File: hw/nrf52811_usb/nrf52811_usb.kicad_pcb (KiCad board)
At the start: 2 copper layers, 80 x 65 mm, 93 parts, among them J1 windrain, J10 Solar Panel, J2 RP_SMA, J3 UART, J4 Battery, J5 Power, J7 AM2315, J8 TC2030-CTX, J9 Therm, Q1 Q_PMOS_GSD, SW1 RST, SW2 RST, U1 MIC550X, U2 NRF52811-QFAA, U3 XBEE_S2C, U5 BMP280, U6 MCP73871, Y1 32.768kHz, Y2 32MHz

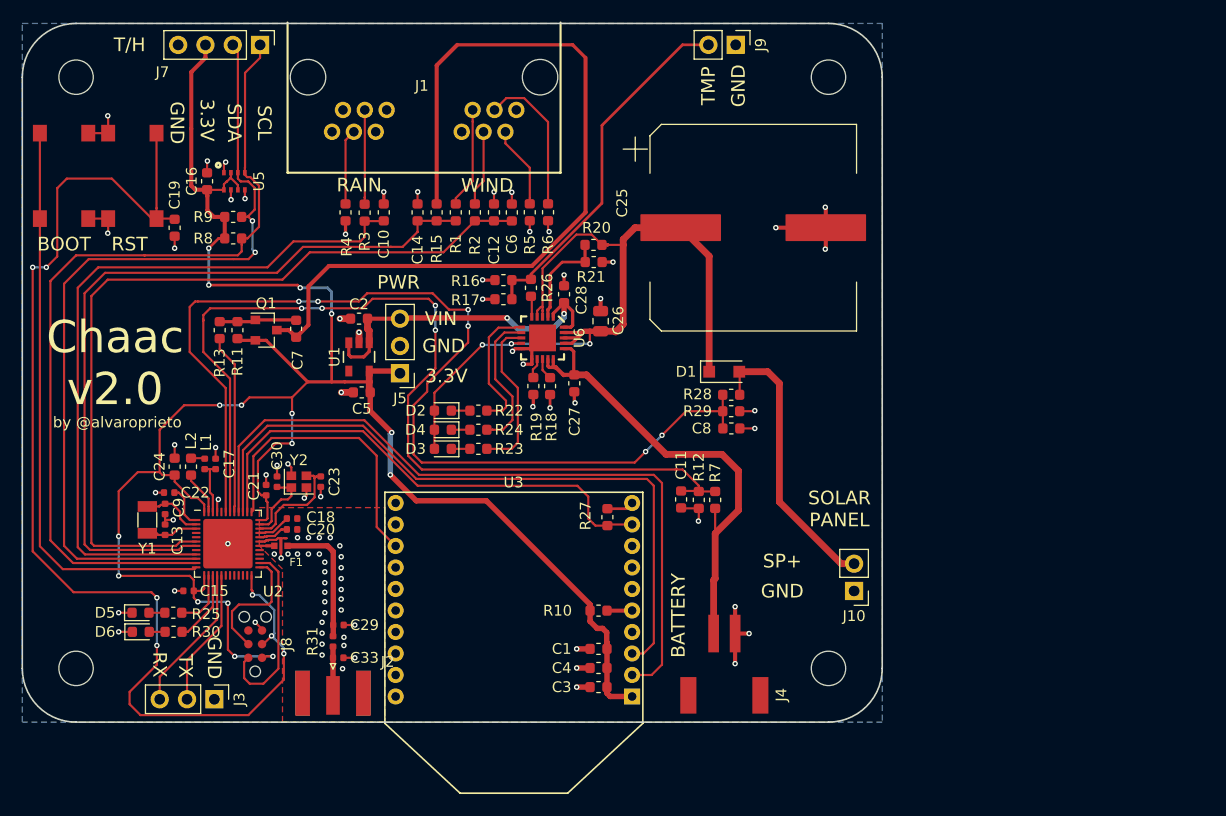
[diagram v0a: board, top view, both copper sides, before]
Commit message: Released nrf52811_usb to oshpark :D
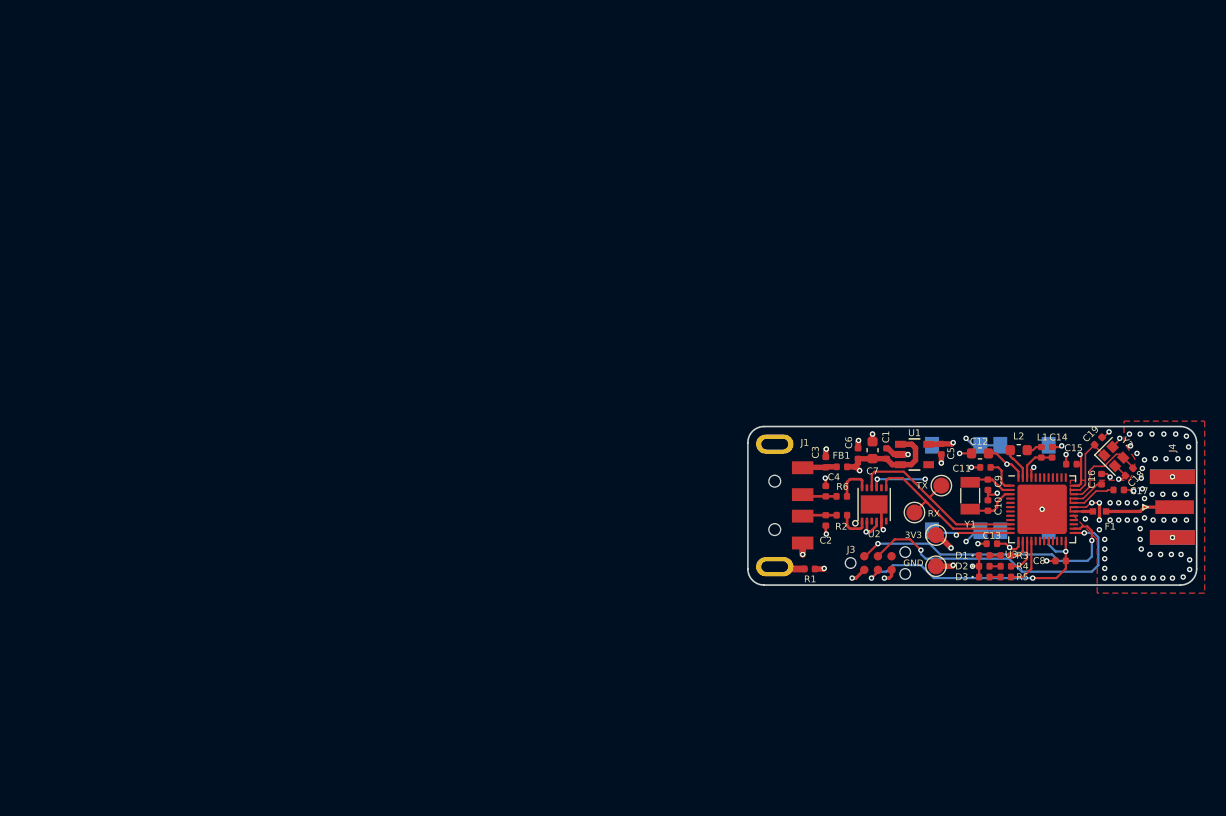
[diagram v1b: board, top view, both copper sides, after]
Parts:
- removed the C10 at (133.6, 62.6)
- removed the C11 at (161.3, 89.3)
- removed the C12 at (143.9, 62.6)
- removed the C14 at (136.8, 62.6)
- removed the C16 at (117.2, 59.7)
- removed the C19 at (114.2, 64.0)
- removed C25: 4700uF, alvarop:CP_Elec_18x16.5
- removed C26: 10uF, Capacitor_SMD:C_0805_2012Metric
- removed C27, C28: 4.7uF, Capacitor_SMD:C_0603_1608Metric
- removed C29, C33: DNP, Capacitor_SMD:C_0402_1005Metric
- removed D4, D5, D6: LED_ALT, LED_SMD:LED_0603_1608Metric
- removed J10: Solar Panel, Connector_PinHeader_2.54mm:PinHeader_1x02_P2.54mm_Vertical
- removed the J3 at (117.9, 107.9)
- removed the J4 at (165.3, 101.8)
- removed J5: Power, Connector_PinHeader_2.54mm:PinHeader_1x03_P2.54mm_Vertical
- removed J7: AM2315, Connector_PinHeader_2.54mm:PinHeader_1x04_P2.54mm_Vertical
- removed J9: Therm, Connector_PinHeader_2.54mm:PinHeader_1x02_P2.54mm_Vertical
- removed Q1: Q_PMOS_GSD, Package_TO_SOT_SMD:SOT-23
- removed R10, R11, R17, R22, R23, R24, R25, R27, R30: 10k, Resistor_SMD:R_0603_1608Metric
- removed R12, R19, R21, R28, R29, R7: 100k, Resistor_SMD:R_0603_1608Metric
- removed R13: 0, Resistor_SMD:R_0603_1608Metric
- removed R15, R8, R9: 4.7k, Resistor_SMD:R_0603_1608Metric
- removed R16: 150k, Resistor_SMD:R_0603_1608Metric
- removed R18: 2k, Resistor_SMD:R_0603_1608Metric
- removed R20: 270k, Resistor_SMD:R_0603_1608Metric
- removed R26: 1k, Resistor_SMD:R_0603_1608Metric
- removed R31: 0, Resistor_SMD:R_0402_1005Metric
- removed REF** (x4): MountingHole_3.2mm_M3, MountingHole:MountingHole_3.2mm_M3
- removed the U3 at (145.7, 98.6)
- removed U5: BMP280, alvarop:BMP280
- removed U6: MCP73871, alvarop:MCP73871
- added FB1: FB, Inductor_SMD:L_0402_1005Metric, F.Cu at (176.2, 86.2)
- added TP1: TX, TestPoint:TestPoint_Pad_D1.5mm, F.Cu at (185.5, 88.0)
- added TP2: RX, TestPoint:TestPoint_Pad_D1.5mm, F.Cu at (183.0, 90.5)
- added TP3: GND, TestPoint:TestPoint_Pad_D1.5mm, F.Cu at (185.0, 95.5)
- added TP4: 3V3, TestPoint:TestPoint_Pad_D1.5mm, F.Cu at (185.0, 92.6)
- added U2: FT234XD, alvarop:FTDI_DFN12, F.Cu at (179.2, 89.8)
- C1, C5, C8: footprint Capacitor_SMD:C_0603_1608Metric -> Capacitor_SMD:C_0402_1005Metric
- C2: value 1uF -> 47pF; footprint Capacitor_SMD:C_0603_1608Metric -> Capacitor_SMD:C_0402_1005Metric
- C3: value 8.2pF -> 10nF; footprint Capacitor_SMD:C_0603_1608Metric -> Capacitor_SMD:C_0402_1005Metric
- C4: value 10uF -> 47pF; footprint Capacitor_SMD:C_0603_1608Metric -> Capacitor_SMD:C_0402_1005Metric
- C6: value 0.01 uF -> 0.1uF; footprint Capacitor_SMD:C_0603_1608Metric -> Capacitor_SMD:C_0402_1005Metric
- C7: value DNP -> 4.7uF
- D1: value MBR120VLSFT1G -> LED_ALT; footprint Diode_SMD:D_SOD-123F -> LED_SMD:LED_0402_1005Metric
- D2, D3: footprint LED_SMD:LED_0603_1608Metric -> LED_SMD:LED_0402_1005Metric
- J1: value windrain -> USB_A; footprint alvarop:043814-6621 -> alvarop:MOLEX-0480371000
- R1: value 1k -> DNP; footprint Resistor_SMD:R_0603_1608Metric -> Resistor_SMD:R_0402_1005Metric
- R2, R6: value 1k -> 27; footprint Resistor_SMD:R_0603_1608Metric -> Resistor_SMD:R_0402_1005Metric
- R3, R4, R5: value 1k -> 10k; footprint Resistor_SMD:R_0603_1608Metric -> Resistor_SMD:R_0402_1005Metric
- SW1: renamed from SW2; moved to B.Cu
- SW2: renamed from SW1; moved to B.Cu
- moved SW1 87.9 mm to (186.9, 88.2), turned to 90 degrees
- moved SW2 87.9 mm to (193.2, 88.2), turned to 270 degrees
- moved J4 80.0 mm to (207.0, 90.0), turned to 0 degrees
- moved L1 77.8 mm to (194.8, 84.9)
- moved C14 77.8 mm to (195.8, 84.9)
- moved L2 77.0 mm to (192.7, 84.7), turned to 180 degrees
- moved C17 77.0 mm to (202.0, 88.4)
- moved C10 76.6 mm to (189.8, 89.8)
- moved C9 76.6 mm to (189.8, 87.9)
- moved Y1 76.6 mm to (188.2, 88.9)
- moved C19 76.5 mm to (200.1, 83.9), turned to 45 degrees
- moved F1 76.2 mm to (200.2, 90.4)
- moved C11 76.0 mm to (189.6, 86.3)
- moved Y2 75.8 mm to (201.5, 85.3), turned to 315 degrees
- moved U3 75.8 mm to (194.9, 90.2)
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- renumbered C13 to C10, C22 to C11, C24 to C12, C15 to C13, C17 to C14, C21 to C15, C18 to C16, C20 to C17, C23 to C18, C30 to C19, J8 to J3, J2 to J4, U2 to U3
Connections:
- C1 pad 1: +3V3 -> /VIN
- C2 pad 1: /VIN -> /USB_DM
- C3 pad 1: +3V3 -> GND
- C3 pad 2: GND -> Net-(C3-Pad2)
- C4 pad 1: +3V3 -> /USB_DP
- C6 pad 1: /WSPEED -> /VIN
- C7 pad 1: /SNS_3V3 -> /VIN
- C7 pad 2: Net-(C7-Pad2) -> GND
- C8 pad 1: /VSOLAR -> /nRST
- D1 pad 1: /MCP_VIN -> GND
- D1 pad 2: /SOLAR_IN -> Net-(D1-Pad2)
- D2 pad 1: Net-(D2-Pad1) -> GND
- D2 pad 2: /MCP_VIN -> Net-(D2-Pad2)
- D3 pad 1: Net-(D3-Pad1) -> GND
- D3 pad 2: /MCP_VIN -> Net-(D3-Pad2)
- F1 pad 3: Net-(C29-Pad1) -> Net-(F1-Pad3)
- J1 pad 1: Net-(J1-Pad1) -> Net-(C3-Pad2)
- J1 pad 2: Net-(J1-Pad2) -> /USB_DP
- J1 pad 3: Net-(J1-Pad3) -> /USB_DM
- J1 pad 4: Net-(J1-Pad4) -> GND
- J4 pad 1: Net-(C33-Pad1) -> Net-(F1-Pad3)
- R1 pad 2: /WDIR -> GND
- R2 pad 1: /WSPEED -> Net-(R2-Pad1)
- R2 pad 2: Net-(J1-Pad4) -> /USB_DM
- R3 pad 1: /RAIN -> Net-(D1-Pad2)
- R3 pad 2: Net-(J1-Pad9) -> /TX_LED
- R4 pad 1: Net-(J1-Pad10) -> Net-(D2-Pad2)
- R4 pad 2: GND -> /RX_LED
- R5 pad 1: GND -> Net-(D3-Pad2)
- R5 pad 2: Net-(J1-Pad2) -> /STATUS_LED
- R6 pad 1: GND -> /USB_DP
- R6 pad 2: Net-(J1-Pad3) -> Net-(R6-Pad2)
- U3 pad 10: /SDA -> /UART_TX
- U3 pad 11: /SCL -> /UART_RX
- U3 pad 14: /LED1 -> /TX_LED
- U3 pad 15: /LED2 -> /RX_LED
- U3 pad 16: /UART_TX -> /STATUS_LED
- U3 pad 17: /UART_RX -> Net-(U3-Pad17)
- U3 pad 37: /XB_ON -> Net-(U3-Pad37)
- U3 pad 38: /XB_nSBY -> Net-(U3-Pad38)
- U3 pad 39: /XB_RX -> Net-(U3-Pad39)
- U3 pad 40: /XB_TX -> Net-(U3-Pad40)
- U3 pad 41: /SNS_3V3_EN -> Net-(U3-Pad41)
- U3 pad 42: /BATT -> Net-(U3-Pad42)
- U3 pad 43: /VSOLAR -> Net-(U3-Pad43)
- U3 pad 6: /WSPEED -> Net-(U3-Pad6)
- U3 pad 7: /WDIR -> Net-(U3-Pad7)
- U3 pad 9: /RAIN -> Net-(U3-Pad9)
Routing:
- net +3V3: track 191.6 -> 21.9 mm, vias 16 -> 8
- net /VSOLAR: track 97.3 -> 0.00 mm, vias 6 -> 0
- net /BATT: track 89.1 -> 0.00 mm, vias 4 -> 0
- net /nRST: track 109.6 -> 26.3 mm, vias 7 -> 3
- net /SCL: track 79.1 -> 0.00 mm
- net /SDA: track 78.4 -> 0.00 mm, vias 2 -> 0
- net /SNS_3V3: track 78.3 -> 0.00 mm
- net /MCP_VIN: track 76.5 -> 0.00 mm, vias 3 -> 0
- net /WSPEED: track 75.0 -> 0.00 mm
- net /WDIR: track 72.2 -> 0.00 mm
- net /XB_TX: track 69.0 -> 0.00 mm
- net /RAIN: track 67.3 -> 0.00 mm
- net /XB_RX: track 64.3 -> 0.00 mm
- net /XB_nSBY: track 46.9 -> 0.00 mm
- net /BOOT: track 53.9 -> 7.54 mm, vias 0 -> 1
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- added copper zone on Power.Cu, net +3V3
- added copper zone on Power.Cu, net /VIN
- added copper zone on GND.Cu, net GND
- removed copper zone on B.Cu, net GND
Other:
- board size 80 x 65 mm -> 41.8 x 14.8 mm
- copper layers 2 -> 4
- rule trace_min: 0.1524 -> 0.127
- board text added: "3V3"
- board text added: "NRF52811_USB by @alvaroprieto"
- board text removed: "3.3V"
- board text removed: "BATTERY"
- board text removed: "Chaac v2.0"
- board text removed: "PWR"
- board text removed: "RAIN"
- board text removed: "SCL"
- board text removed: "SDA"
- board text removed: "SOLAR PANEL"
- board text removed: "SP+"
- board text removed: "T/H"
- board text removed: "TMP"
- board text removed: "VIN"
- board text removed: "WIND"
- board text removed: "by @alvaroprieto"
